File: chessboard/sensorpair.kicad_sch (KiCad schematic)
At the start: 4 parts, among them U23 MMC5603NJ, U24 MMC5603NJ

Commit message: a
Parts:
- added C77: 100nF, Capacitor_SMD:C_0805_2012Metric_Pad1.18x1.45mm_HandSolder, symbol Device:C
- C78: renamed from C22; footprint (none) -> Capacitor_SMD:C_0805_2012Metric_Pad1.18x1.45mm_HandSolder
- renumbered RN7 to RN31, U23 to U32, U24 to U33
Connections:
- net +3.3V: now also C77.1
- net C0: now also RN31.7 (R2.2), U32.A2 (SCL); no longer RN31.5 (R4.2), U33.A2 (SCL)
- net C1: now also RN31.5 (R4.2), U33.A2 (SCL); no longer RN31.7 (R2.2), U32.A2 (SCL)
- net D0: now also RN31.8 (R1.2), U32.B2 (SDA); no longer RN31.6 (R3.2), U33.B2 (SDA)
- net D1: now also RN31.6 (R3.2), U33.B2 (SDA); no longer RN31.8 (R1.2), U32.B2 (SDA)
- net GND: now also C77.2
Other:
- moved on the sheet: C78, RN31, U32, U33

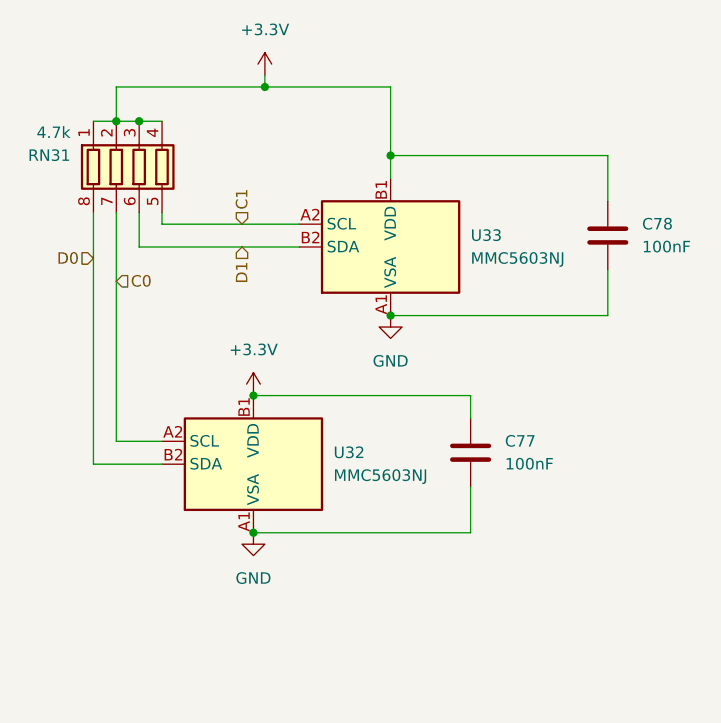
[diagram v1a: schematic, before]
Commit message: new single row board
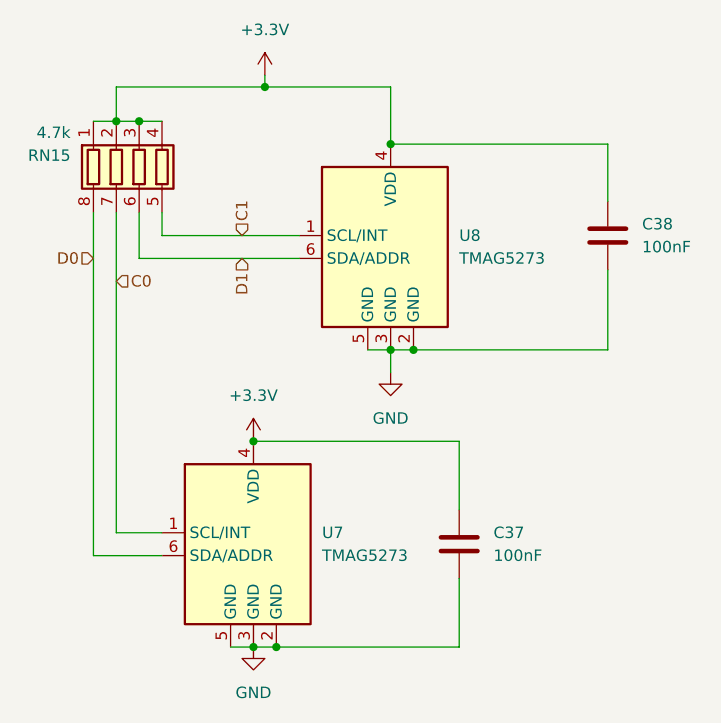
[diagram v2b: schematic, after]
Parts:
- removed U32, U33: MMC5603NJ, Package_BGA:WLP-4_0.86x0.86mm_P0.4mm, symbol Sensor_Magnetic:MMC5633NJL
- added U7, U8: TMAG5273, Package_TO_SOT_SMD:SOT-23-6, symbol Sensor_Magnetic:TLV493D
- RN15: renamed from RN31; footprint Resistor_SMD:R_Array_Concave_4x0603 -> Resistor_SMD:R_Array_Convex_4x0603; LCSC (none) -> C1980
- renumbered C77 to C37, C78 to C38
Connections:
- net +3.3V: now also U7.4 (VDD), U8.4 (VDD)
- net C0: now also U7.1 (SCL/INT)
- net C1: now also U8.1 (SCL/INT)
- net D0: now also U7.6 (SDA/ADDR)
- net D1: now also U8.6 (SDA/ADDR)
- net GND: now also U7.2 (GND), U7.3 (GND), U7.5 (GND), U8.2 (GND), U8.3 (GND), U8.5 (GND)
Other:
- moved on the sheet: C37

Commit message: make it pretty
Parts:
- renumbered C37 to C5, C38 to C6, RN15 to RN2, U7 to U2, U8 to U3
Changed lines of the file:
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@@
   (symbol (lib_id "Sensor_Magnetic:TLV493D") (at 92.71 85.09 0) (unit 1)
     (in_bom yes) (on_board yes) (dnp no) (fields_autoplaced)
-    (property "Reference" "U7" (at 100.33 82.55 0)
+    (property "Reference" "U2" (at 100.33 82.55 0)
       (effects (font (size 1.27 1.27)) (justify left))
     )
@@
   (symbol (lib_id "power:+3.3V") (at 93.98 31.75 0) (unit 1)
     (in_bom yes) (on_board yes) (dnp no) (fields_autoplaced)
-    (property "Reference" "#PWR0116" (at 93.98 35.56 0)
+    (property "Reference" "#PWR029" (at 93.98 35.56 0)
       (effects (font (size 1.27 1.27)) hide)
     )
@@
   (symbol (lib_id "power:GND") (at 92.71 95.25 0) (unit 1)
     (in_bom yes) (on_board yes) (dnp no) (fields_autoplaced)
-    (property "Reference" "#PWR0115" (at 92.71 101.6 0)
+    (property "Reference" "#PWR028" (at 92.71 101.6 0)
       (effects (font (size 1.27 1.27)) hide)
     )
@@
   (symbol (lib_id "Device:R_Pack04") (at 80.01 41.91 0) (mirror x) (unit 1)
     (in_bom yes) (on_board yes) (dnp no)
-    (property "Reference" "RN15" (at 72.39 40.64 0)
+    (property "Reference" "RN2" (at 72.39 40.64 0)
       (effects (font (size 1.27 1.27)) (justify right))
     )
@@
   (symbol (lib_id "Device:C") (at 132.08 49.53 0) (unit 1)
     (in_bom yes) (on_board yes) (dnp no) (fields_autoplaced)
-    (property "Reference" "C38" (at 135.89 48.26 0)
+    (property "Reference" "C6" (at 135.89 48.26 0)
       (effects (font (size 1.27 1.27)) (justify left))
     )
@@
   (symbol (lib_id "Device:C") (at 115.57 83.82 0) (unit 1)
     (in_bom yes) (on_board yes) (dnp no) (fields_autoplaced)
-    (property "Reference" "C37" (at 119.38 82.55 0)
+    (property "Reference" "C5" (at 119.38 82.55 0)
       (effects (font (size 1.27 1.27)) (justify left))
     )
@@
   (symbol (lib_id "power:GND") (at 107.95 64.77 0) (unit 1)
     (in_bom yes) (on_board yes) (dnp no)
-    (property "Reference" "#PWR0117" (at 107.95 71.12 0)
+    (property "Reference" "#PWR030" (at 107.95 71.12 0)
       (effects (font (size 1.27 1.27)) hide)
     )
@@
   (symbol (lib_id "power:+3.3V") (at 92.71 72.39 0) (unit 1)
     (in_bom yes) (on_board yes) (dnp no) (fields_autoplaced)
-    (property "Reference" "#PWR0114" (at 92.71 76.2 0)
+    (property "Reference" "#PWR027" (at 92.71 76.2 0)
       (effects (font (size 1.27 1.27)) hide)
     )
@@
   (symbol (lib_id "Sensor_Magnetic:TLV493D") (at 107.95 52.07 0) (unit 1)
     (in_bom yes) (on_board yes) (dnp no) (fields_autoplaced)
-    (property "Reference" "U8" (at 115.57 49.53 0)
-      (effects (font (size 1.27 1.27)) (justify left))
-    )
+    (property "Reference" "U3" (at 115.57 49.53 0)
+      (effects (font (size 1.27 1.27)) (justify left))
+    )
